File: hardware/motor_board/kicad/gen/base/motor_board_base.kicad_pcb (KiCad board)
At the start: 4 copper layers, 75 x 35 mm, 237 parts, among them J1 BOOMELE_1.27-2x10P, J2 WAFER-SH1.0-6PWB, J3 WAFER-SH1.0-6PWB, J4 S5B-XH-A, Q1 HYG015N04LS1C2, Q2 HYG015N04LS1C2, Q3 HYG015N04LS1C2, Q4 HYG015N04LS1C2, Q5 HYG015N04LS1C2, Q6 HYG015N04LS1C2, Q7 HYG015N04LS1C2, Q8 HYG015N04LS1C2, U1 STM32G474RET6, U10 SN74LVC3G17DCUR, U11 TPS22945DCKR, U12 TPS22945DCKR, U13 LM74502DDFR, U14 74LVC1G17SE-7, U2 DRV8323RHRGZR, U3 DRV8316CRRGFR, U4 DRV8316CRRGFR, U5 AP2112K-3.3TRG1, U6 SN74LVC08APWR, U7 INA239AIDGSR, U8 BQ76907RGRR, U9 SN74LVC3G17DCUR

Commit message: motor_board: go to 6 layers (F / L2 GND / L3 VBAT feed + lanes / L4 signals / L5 GND / B)
Base edit sets 6 copper layers, adds the L5 GND plane (copy of L2's), writes a 1.6 mm
1 oz stack-up; router, geo, geom_export, apply_routes, layout_check know In3/In4.
Everything routed keeps its layer. DRC 0, 220 unconnected.

Co-Authored-By: Claude Opus 5.5 (1M context) <noreply@anthropic.com>
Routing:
- added copper zone on In4.Cu, net GND
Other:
- copper layers 4 -> 6
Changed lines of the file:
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@@
 		(4 "In1.Cu" signal "L2.GND")
 		(6 "In2.Cu" signal "L3.PWR+SIG")
+		(8 "In3.Cu" signal "L4.SIG")
+		(10 "In4.Cu" signal "L5.GND")
 		(2 "B.Cu" signal)
 		(9 "F.Adhes" user "F.Adhesive")
@@
 	(setup
 		(stackup
-			(layer "F.SilkS"
-				(type "Top Silk Screen")
-			)
-			(layer "F.Paste"
-				(type "Top Solder Paste")
-			)
-			(layer "F.Mask"
-				(type "Top Solder Mask")
-				(thickness 0.01)
-			)
-			(layer "F.Cu"
-				(type "copper")
-				(thickness 0.035)
-			)
-			(layer "dielectric 1"
-				(type "prepreg")
-				(thickness 0.2104)
-				(material "7628")
-				(epsilon_r 4.4)
-				(loss_tangent 0.02)
-			)
-			(layer "In1.Cu"
-				(type "copper")
-				(thickness 0.035)
-			)
-			(layer "dielectric 2"
-				(type "core")
-				(thickness 1.065)
-				(material "FR4")
-				(epsilon_r 4.6)
-				(loss_tangent 0.02)
-			)
-			(layer "In2.Cu"
-				(type "copper")
-				(thickness 0.035)
-			)
-			(layer "dielectric 3"
-				(type "prepreg")
-				(thickness 0.2104)
-				(material "7628")
-				(epsilon_r 4.4)
-				(loss_tangent 0.02)
-			)
-			(layer "B.Cu"
-				(type "copper")
-				(thickness 0.035)
-			)
-			(layer "B.Mask"
-				(type "Bottom Solder Mask")
-				(thickness 0.01)
-			)
-			(layer "B.Paste"
-				(type "Bottom Solder Paste")
-			)
-			(layer "B.SilkS"
-				(type "Bottom Silk Screen")
-			)
+			(layer "F.SilkS" (type "Top Silk Screen"))
+			(layer "F.Paste" (type "Top Solder Paste"))
+			(layer "F.Mask" (type "Top Solder Mask") (thickness 0.01))
+			(layer "F.Cu" (type "copper") (thickness 0.035))
+			(layer "dielectric 1" (type "prepreg") (thickness 0.2) (material "FR4") (epsilon_r 4.4) (loss_tangent 0.02))
+			(layer "In1.Cu" (type "copper") (thickness 0.035))
+			(layer "dielectric 2" (type "core") (thickness 0.3) (material "FR4") (epsilon_r 4.6) (loss_tangent 0.02))
+			(layer "In2.Cu" (type "copper") (thickness 0.035))
+			(layer "dielectric 3" (type "prepreg") (thickness 0.37) (material "FR4") (epsilon_r 4.4) (loss_tangent 0.02))
+			(layer "In3.Cu" (type "copper") (thickness 0.035))
+			(layer "dielectric 4" (type "core") (thickness 0.3) (material "FR4") (epsilon_r 4.6) (loss_tangent 0.02))
+			(layer "In4.Cu" (type "copper") (thickness 0.035))
+			(layer "dielectric 5" (type "prepreg") (thickness 0.2) (material "FR4") (epsilon_r 4.4) (loss_tangent 0.02))
+			(layer "B.Cu" (type "copper") (thickness 0.035))
+			(layer "B.Mask" (type "Bottom Solder Mask") (thickness 0.01))
+			(layer "B.Paste" (type "Bottom Solder Paste"))
+			(layer "B.SilkS" (type "Bottom Silk Screen"))
 			(copper_finish "ENIG")
 			(dielectric_constraints no)
@@
 			)
 		)
+	)
+	(zone
+		(net "GND")
+		(layer "In4.Cu")
+		(name "L5 GND plane")
+		(hatch edge 0.5)
+		(connect_pads thru_hole_only
+			(clearance 0.2)
+		)
+		(min_thickness 0.2)
+		(fill yes
+			(thermal_gap 0.5)
+			(thermal_bridge_width 1)
+			(island_removal_mode 0)
+		)
+		(polygon
+			(pts
+				(xy 100.25 70.25) (xy 174.75 70.25) (xy 174.75 104.75) (xy 100.25 104.75)
+			)
+		)

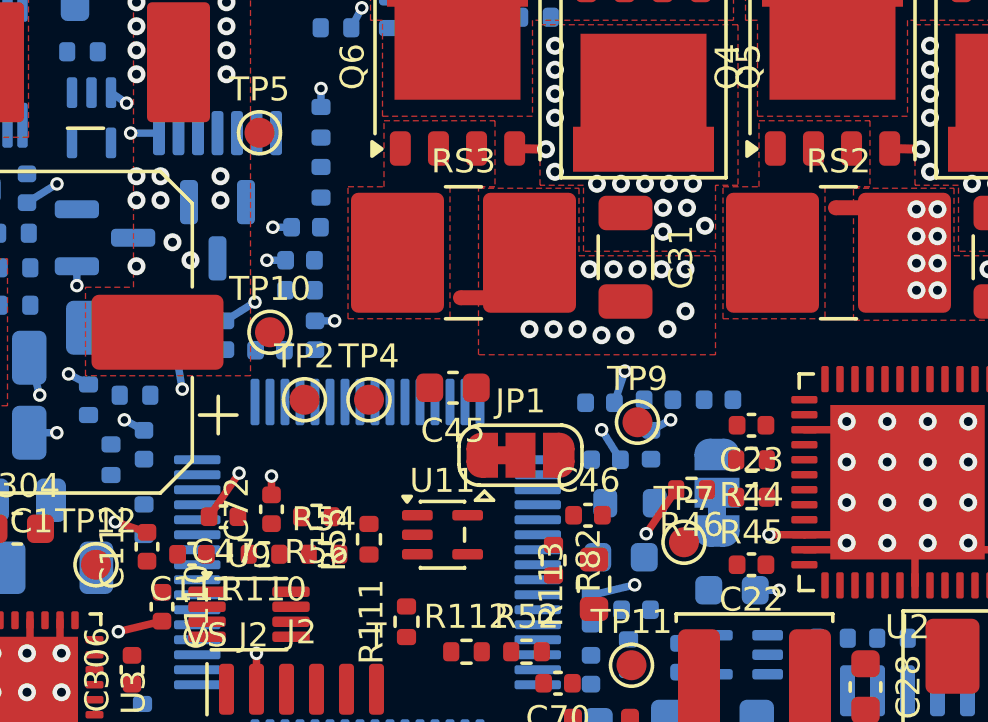
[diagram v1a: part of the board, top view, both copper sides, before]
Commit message: motor_board routing 12a/12b0/12b: U2 west escapes, U6 escape, U2 rear bus on L4, hub nets on L4
U2 pins 28/33 escape west between the mode resistors (redundant pin-34 GND via dropped);
U6's signal pins escape between its rows / into the VBAT via row gap (RS4's VBAT pad is
over U6's middle; D7 nudged 0.6 mm; R63 takes its own VBAT via); U1 pins 8/9 out north;
the six U2 rear lines fanned out by hand into lane order INLC/INLB/INLA | INHA | INHB/INHC
and routed inside-out on L4 (17-28 mm, INLC 41 mm). DRC 0, 235 unconnected.

Co-Authored-By: Claude Opus 5.5 (1M context) <noreply@anthropic.com>
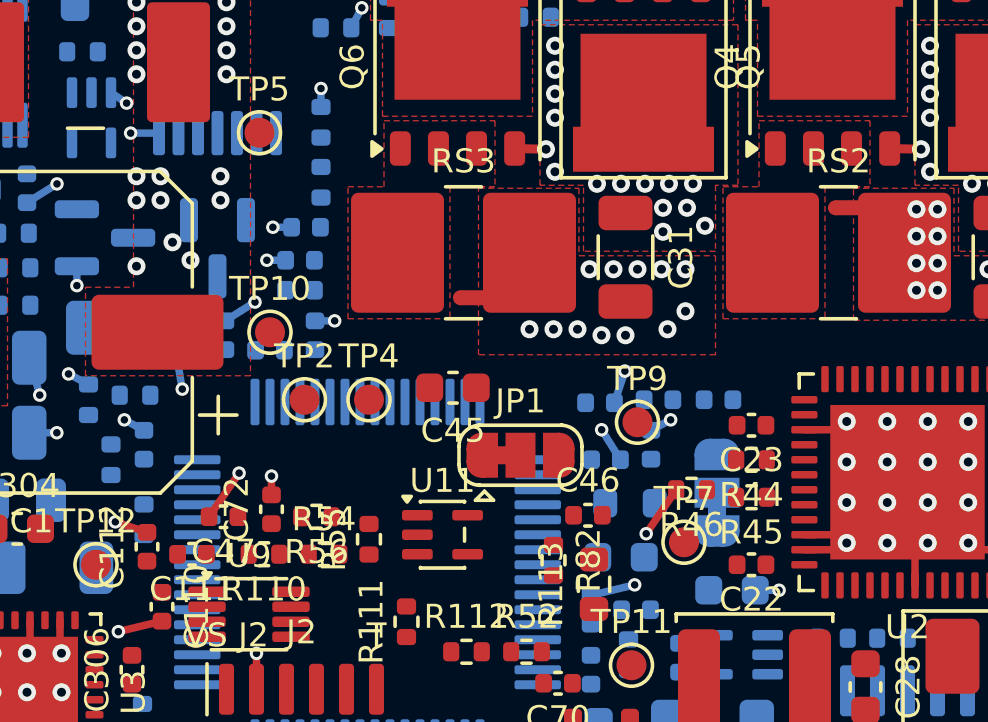
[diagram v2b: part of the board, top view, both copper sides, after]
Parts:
- moved D7 0.60 mm to (130.5, 85.2)
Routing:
- net GND: track 70.0 -> 68.9 mm
- net VBAT: vias 49 -> 48
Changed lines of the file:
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@@
 	(footprint "Package_TO_SOT_SMD:SOT-23"
 		(layer "B.Cu")
-		(at 130.5 84.6 -90)
+		(at 130.5 85.2 -90)
 		(descr "SOT, 3 Pin (JEDEC TO-236 Var AB https://www.jedec.org/document_search?search_api_views_fulltext=TO-236)")
 		(tags "SOT TO_SOT_SMD")
@@
 	)
 	(via
-		(at 129 84.999999)
-		(size 0.6)
-		(drill 0.3)
-		(layers "F.Cu" "B.Cu")
-		(net "VBAT")
-	)
-	(via
 		(at 155.65 83.049999)
 		(size 0.6)
@@
 	)
 	(segment
-		(start 150.0625 94.75)
-		(end 148.88 94.75)
-		(width 0.25)
-		(layer "F.Cu")
-		(net "GND")
-	)
-	(segment
 		(start 150.0625 91.25)
 		(end 151.125 91.25)
@@
 	)
 	(via
-		(at 148.88 94.75)
-		(size 0.45)
-		(drill 0.25)
-		(layers "F.Cu" "B.Cu")
-		(net "GND")
-	)
-	(via
 		(at 131.219999 92.695)
 		(size 0.45)
@@
 		(size 0.6)
 		(drill 0.3)
+		(layers "F.Cu" "B.Cu")
+		(net "GND")
+	)
+	(via
+		(at 129 84.999999)
+		(size 0.6)
+		(drill 0.3)

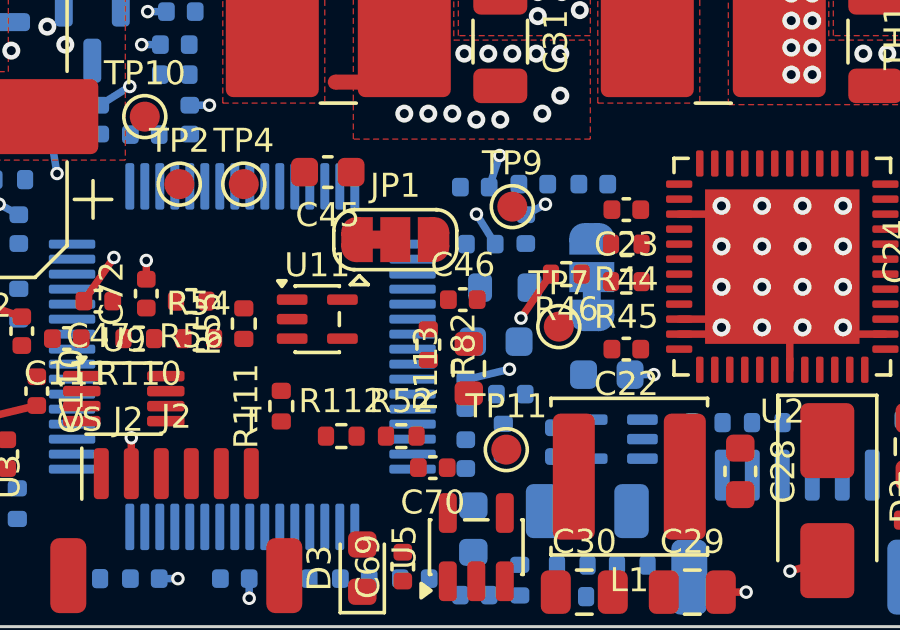
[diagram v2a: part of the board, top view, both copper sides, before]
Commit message: motor_board routing: hall outputs R_S1-3 and L_S3 routed; hand escapes become early reservations
Hand-placed escapes (U2 west, U6, U1 pins 8/9/24, U2 rear fan-out) now go in right after
block 7d so router blocks route around them; R_SOC routed after the U2 rear bus (it
crosses the INL lanes topologically); U1 pin 24 escape between U1's pads and C66 (east
bus north-group columns moved 0.65 mm east, R113 0.35 mm east); part nudges made
absolute (D7 had been shifted twice). DRC 0, 235 unconnected.

Co-Authored-By: Claude Opus 5.5 (1M context) <noreply@anthropic.com>
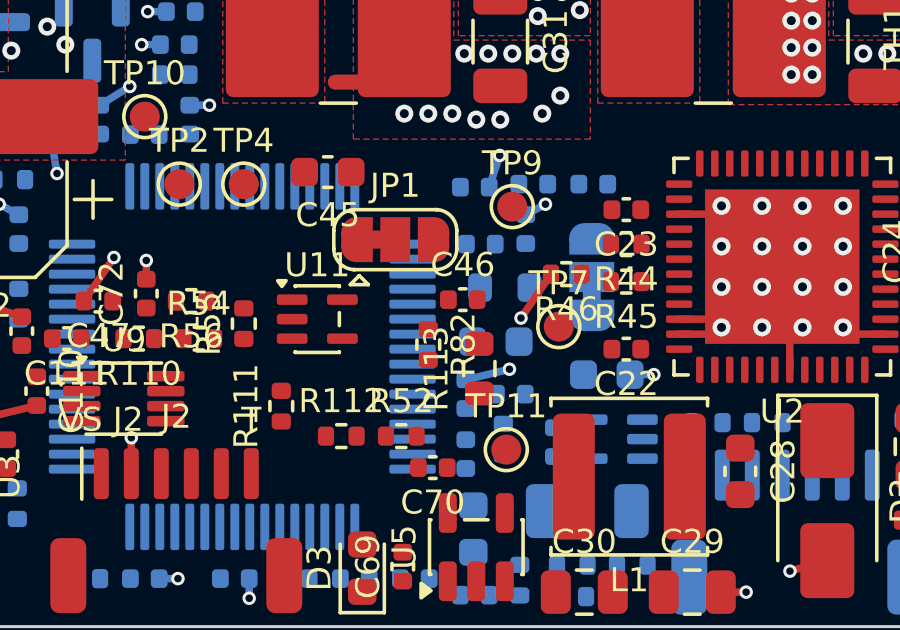
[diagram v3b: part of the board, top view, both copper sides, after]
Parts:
- moved R113 0.35 mm to (143.4, 96.4)
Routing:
- net GND: track 68.9 -> 67.7 mm, vias 151 -> 150
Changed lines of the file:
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@@
 	(footprint "Resistor_SMD:R_0603_1608Metric"
 		(layer "F.Cu")
-		(at 143.05 96.4 90)
+		(at 143.4 96.4 90)
 		(descr "Resistor SMD 0603 (1608 Metric), square (rectangular) end terminal, IPC-7351 nominal, (Body size source: IPC-SM-782 page 72, https://www.pcb-3d.com/wordpress/wp-content/uploads/ipc-sm-782a_amendment_1_and_2.pdf)")
 		(tags "resistor")
@@
 	)
 	(via
-		(at 143.305 91.25)
-		(size 0.45)
-		(drill 0.25)
-		(layers "F.Cu" "B.Cu")
-		(net "GND")
-	)
-	(via
 		(at 120.7 101.3)
 		(size 0.6)
@@
 		(width 0.25)
 		(layer "B.Cu")
-		(net "GND")
-	)
-	(segment
-		(start 143.93 92.25)
-		(end 143.305 91.25)
-		(width 0.25)
-		(layer "B.Cu")

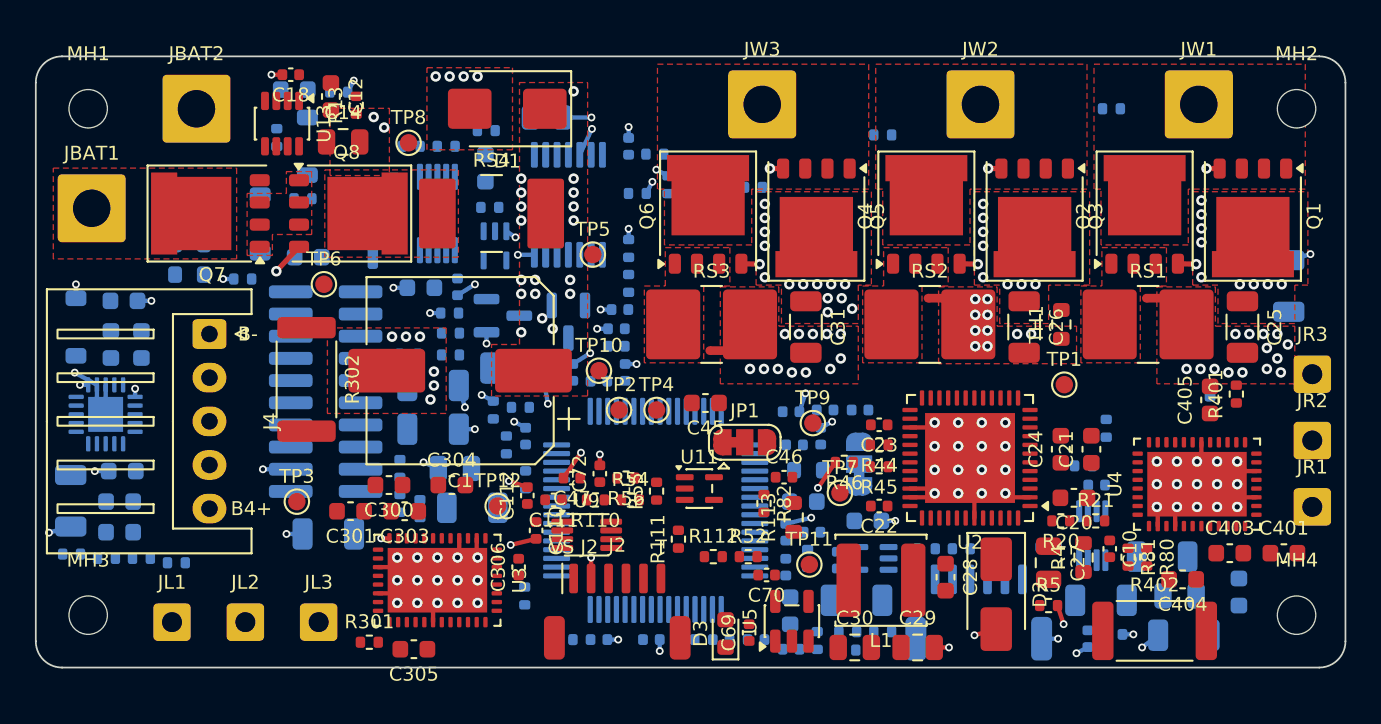
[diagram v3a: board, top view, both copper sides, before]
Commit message: motor_board close-out start: GND pad vias refreshed (+retry), F/B GND fills (lowest priority, router ignores them), pack GND pours to priority 1; DRC 0, 131 open
Co-Authored-By: Claude Opus 5.5 (1M context) <noreply@anthropic.com>
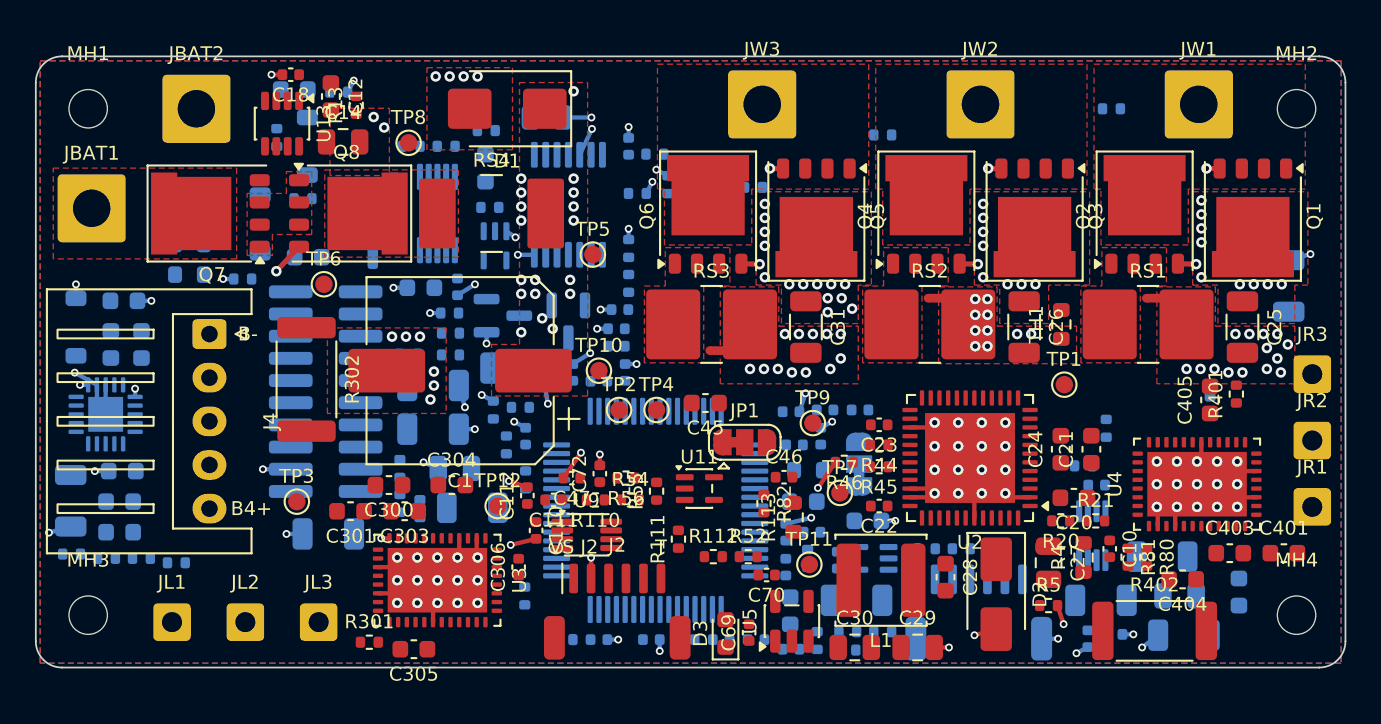
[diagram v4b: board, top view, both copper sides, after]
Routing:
- added copper zone on B.Cu, net GND
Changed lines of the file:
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@@
 		(name "pack: GND at D1")
 		(hatch edge 0.5)
+		(priority 1)
 		(connect_pads thru_hole_only
 			(clearance 0.2)
@@
 		(name "pack: GND at C1")
 		(hatch edge 0.5)
+		(priority 1)
 		(connect_pads thru_hole_only
 			(clearance 0.2)
@@
 		(name "pack: GND at C14")
 		(hatch edge 0.5)
+		(priority 1)
 		(connect_pads thru_hole_only
 			(clearance 0.2)
@@
 			(pts
 				(xy 116.85 72.975) (xy 120.25 72.975) (xy 120.25 76.825) (xy 116.85 76.825)
+			)
+		)
+	)
+	(zone
+		(net "GND")
+		(layer "F.Cu")
+		(name "F GND fill")
+		(hatch edge 0.5)
+		(connect_pads yes
+			(clearance 0.2)
+		)
+		(min_thickness 0.2)
+		(fill yes
+			(thermal_gap 0.5)
+			(thermal_bridge_width 0.5)
+			(island_removal_mode 0)
+		)
+		(polygon
+			(pts
+				(xy 100.25 70.25) (xy 174.75 70.25) (xy 174.75 104.75) (xy 100.25 104.75)
 			)
 		)
@@
 			)
 		)
+	)
+	(zone
+		(net "GND")
+		(layer "B.Cu")
+		(name "B GND fill")
+		(hatch edge 0.5)
+		(connect_pads yes
+			(clearance 0.2)
+		)
+		(min_thickness 0.2)
+		(fill yes
+			(thermal_gap 0.5)
+			(thermal_bridge_width 0.5)
+			(island_removal_mode 0)
+		)
+		(polygon
+			(pts
+				(xy 100.25 70.25) (xy 174.75 70.25) (xy 174.75 104.75) (xy 100.25 104.75)
+			)
+		)

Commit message: C112 beside U9 pin 6; U1 pins 59/60 (L_nFAULT/L_INHA) outward escapes; optional rip-up diagnostic; DRC 0, 89 open
Co-Authored-By: Claude Opus 5.5 (1M context) <noreply@anthropic.com>
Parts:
- moved C112 7.00 mm to (134.9, 97.0), turned to 0 degrees
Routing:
- net GND: track 67.7 -> 66.6 mm, vias 150 -> 149
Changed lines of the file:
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@@
 	(footprint "Capacitor_SMD:C_0402_1005Metric"
 		(layer "F.Cu")
-		(at 128.15 95.15 90)
+		(at 134.9 97)
 		(descr "Capacitor SMD 0402 (1005 Metric), square (rectangular) end terminal, IPC-7351 nominal, (Body size source: IPC-SM-782 page 76, https://www.pcb-3d.com/wordpress/wp-content/uploads/ipc-sm-782a_amendment_1_and_2.pdf)")
 		(tags "capacitor")
 		(property "Reference" "C112"
-			(at 0 -1.16 90)
+			(at 0 -1.16 0)
 			(layer "F.SilkS")
 			(effects
@@
 		)
 		(property "Value" "1nF 50V"
-			(at 0 1.16 90)
+			(at 0 1.16 0)
 			(layer "F.Fab")
 			(hide yes)
@@
 		)
 		(property "Datasheet" ""
-			(at 0 0 90)
+			(at 0 0 0)
 			(layer "F.Fab")
 			(hide yes)
@@
 		)
 		(property "Description" "Unpolarized capacitor"
-			(at 0 0 90)
+			(at 0 0 0)
 			(layer "F.Fab")
 			(hide yes)
@@
 		)
 		(property "KiLib_Generator" "SMD_2terminal_chip_molded"
-			(at 0 0 90)
+			(at 0 0 0)
 			(layer "F.SilkS")
 			(hide yes)
@@
 		)
 		(property "LCSC" "C1523"
-			(at 0 0 90)
+			(at 0 0 0)
 			(layer "F.SilkS")
 			(hide yes)
@@
 		)
 		(fp_text user "${REFERENCE}"
-			(at 0 0 90)
+			(at 0 0 0)
 			(layer "F.Fab")
 			(effects
@@
 		)
 		(pad "1" smd roundrect
-			(at -0.48 0 90)
+			(at -0.48 0)
 			(size 0.56 0.62)
 			(layers "F.Cu" "F.Mask" "F.Paste")
@@
 		)
 		(pad "2" smd roundrect
-			(at 0.48 0 90)
+			(at 0.48 0)
 			(size 0.56 0.62)
 			(layers "F.Cu" "F.Mask" "F.Paste")
@@
 	)
 	(segment
-		(start 128.15 94.67)
-		(end 127.095 94.32)
-		(width 0.25)
-		(layer "F.Cu")
-		(net "GND")
-	)
-	(segment
 		(start 151.45 103.85)
 		(end 152.295 103.85)
@@
 		(layers "F.Cu" "B.Cu")
 		(net "GND")
-	)
-	(via
-		(at 127.095 94.32)
-		(size 0.45)
-		(drill 0.25)
-		(layers "F.Cu" "B.Cu")
-		(net "GND")

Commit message: U3 right-column escapes by hand (SOA/SOB/SOC vias, AVDD straight into C306), out of the drifting auto fan-out; C110's GND via dropped for it; DRC 0, 90 open
Co-Authored-By: Claude Opus 5.5 (1M context) <noreply@anthropic.com>
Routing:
- net GND: track 66.6 -> 65.1 mm, vias 149 -> 148
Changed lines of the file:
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@@
-	)
-	(segment
-		(start 128.65 97.63)
-		(end 127.195 97.979999)
-		(width 0.25)
-		(layer "F.Cu")
-		(net "GND")
 	)
 	(segment
@@
 		(layers "F.Cu" "B.Cu")
 		(net "GND")
-	)
-	(via
-		(at 127.195 97.979999)
-		(size 0.45)
-		(drill 0.25)
-		(layers "F.Cu" "B.Cu")
-		(net "GND")
